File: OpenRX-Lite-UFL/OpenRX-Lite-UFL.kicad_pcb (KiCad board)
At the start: 6 copper layers, 8.5 x 12.3 mm, 39 parts, among them U1 ESP32-C3FH4, U2 TLV75533PDQNR, U3 SX1281IMLTRT, X1 CJ17-400001010B20

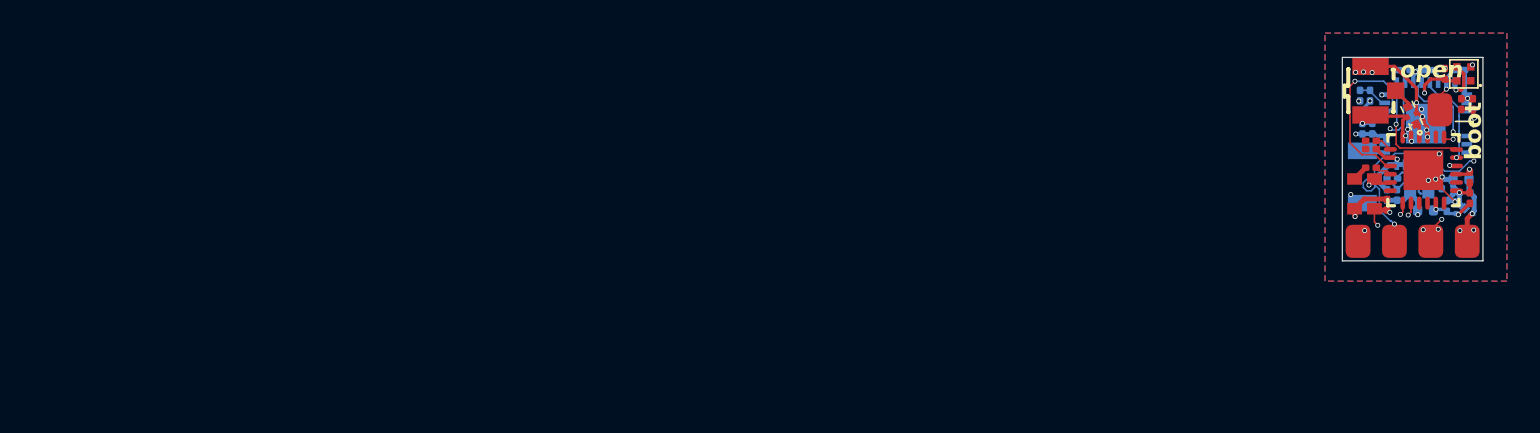
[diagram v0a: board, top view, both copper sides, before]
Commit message: OpenRX Lite (UFL + molex)
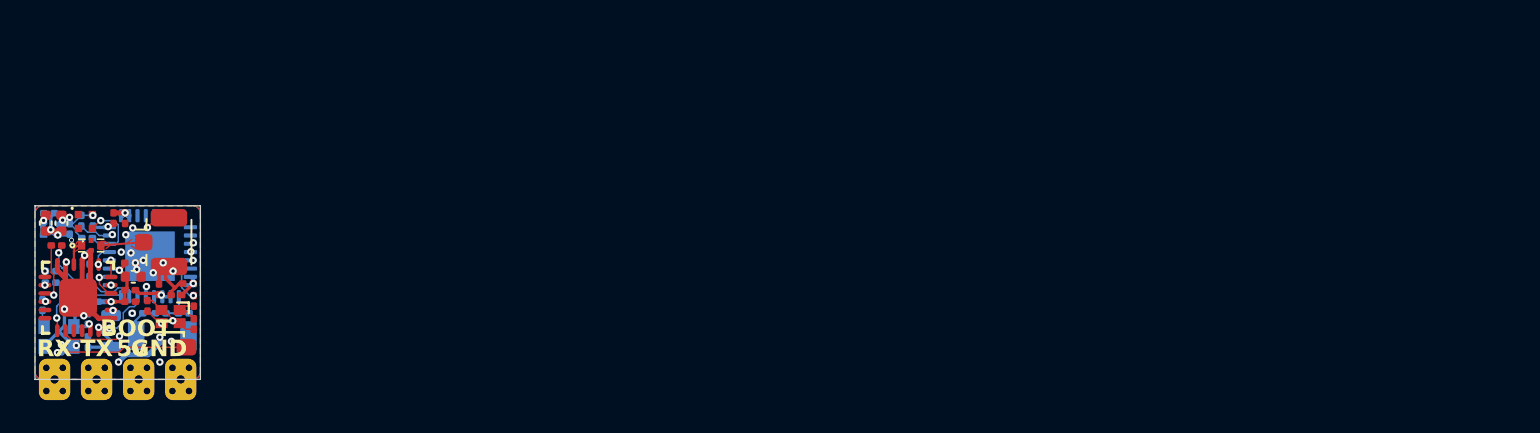
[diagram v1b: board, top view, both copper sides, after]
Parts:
- removed C18, C7: 100nF, Capacitor_SMD:C_0201_0603Metric
- removed C2: 1uF, Capacitor_SMD:C_0201_0603Metric
- removed JP1: U.FL-R-SMT-1(80), OpenRX-Shared:RF-SMD_FRF05002-JSS103M
- removed R1: 10k, Resistor_SMD:R_0201_0603Metric
- added C21: 1.2pF, Capacitor_SMD:C_0201_0603Metric, B.Cu at (106.2, 106.0)
- added C22: 1.2pF, Capacitor_SMD:C_0201_0603Metric, B.Cu at (109.0, 106.0)
- added C23: 1uF, Capacitor_SMD:C_0201_0603Metric, F.Cu at (105.5, 100.2)
- added C24: 10nF, Capacitor_SMD:C_0201_0603Metric, F.Cu at (109.2, 104.2)
- added C25: 1uF, Capacitor_SMD:C_0201_0603Metric, F.Cu at (107.5, 104.5)
- added C26: 10nF, Capacitor_SMD:C_0201_0603Metric, B.Cu at (101.0, 104.2)
- added C27: 10nF, Capacitor_SMD:C_0201_0603Metric, B.Cu at (101.0, 103.5)
- added C28: 1uF, Capacitor_SMD:C_0201_0603Metric, B.Cu at (103.3, 102.7)
- added J1: Conn_Coaxial, Connector_Coaxial:U.FL_Hirose_U.FL-R-SMT-1_Vertical, F.Cu at (108.1, 101.7)
- added L2: 2.5nH, Inductor_SMD:L_0201_0603Metric, B.Cu at (107.6, 106.0)
- added L3: 2.0nH, Inductor_SMD:L_0201_0603Metric, F.Cu at (105.8, 104.6)
- added L4: 15uH, Inductor_SMD:L_0805_2012Metric, B.Cu at (104.6, 107.1)
- added R5: 10k, Resistor_SMD:R_0201_0603Metric, B.Cu at (103.3, 104.1)
- C1, C3: value 18pF -> 15pF; moved to F.Cu
- C11: value 100nF -> 10uF; footprint Capacitor_SMD:C_0201_0603Metric -> Capacitor_SMD:C_0402_1005Metric
- C13, C14, C17, C19, C20, OSC1: moved to B.Cu
- C16, C4, C5, C6, C8, L1, R2, X1: moved to F.Cu
- TP5: value GND -> BOOT
- U1: value ESP32-C3FH4 -> ESP32-C3; footprint OpenRX-Shared:QFN-32_L5.0-W5.0-P0.50-TL-EP3.7 -> Package_DFN_QFN:QFN-32-1EP_5x5mm_P0.5mm_EP3.7x3.7mm
- moved C8 85.6 mm to (100.7, 100.5), turned to -90 degrees
- moved C10 85.6 mm to (100.8, 100.0), turned to 0 degrees
- moved U2 85.5 mm to (101.0, 101.0), turned to 180 degrees
- moved D1 83.8 mm to (103.0, 100.5), turned to 0 degrees
- moved R4 83.8 mm to (102.8, 100.4), turned to -90 degrees
- moved C17 83.6 mm to (103.5, 105.3), turned to 180 degrees
- moved C15 83.3 mm to (102.1, 100.9), turned to -90 degrees
- moved C16 82.5 mm to (101.6, 100.5), turned to -90 degrees
- moved C9 82.1 mm to (105.8, 105.3), turned to 0 degrees
- moved R3 81.7 mm to (103.2, 101.5)
- moved U3 81.7 mm to (102.6, 105.0)
- moved C11 81.0 mm to (105.9, 103.8), turned to 0 degrees
- moved TP3 80.8 mm to (106.3, 110.0), turned to 0 degrees
- moved C19 80.8 mm to (100.5, 105.5), turned to 90 degrees
- moved FL1 80.2 mm to (103.4, 101.9), turned to 0 degrees
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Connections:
- net /ESP32-C3 + SX1281 Core (UFL)/CHIP_BOOT renamed /ESP32-C3 + SX1281 Core (UFL)/BOOT
- C20 pad 1: Net-(U3-VR_PA) -> GND
- C20 pad 2: GND -> Net-(U3-DCC_FB)
- D1 pad 2: +5V -> +3V3
- R3 pad 2: /ESP32-C3 + SX1281 Core (UFL)/NSS -> /ESP32-C3 + SX1281 Core (UFL)/LED
- U1 pad 1: /ESP32-C3 + SX1281 Core (UFL)/WIFI -> Net-(U1-LNA_IN)
- U1 pad 10: /ESP32-C3 + SX1281 Core (UFL)/DIO1 -> /ESP32-C3 + SX1281 Core (UFL)/MISO
- U1 pad 12: /ESP32-C3 + SX1281 Core (UFL)/MISO -> /ESP32-C3 + SX1281 Core (UFL)/SCK
- U1 pad 13: /ESP32-C3 + SX1281 Core (UFL)/MOSI -> /ESP32-C3 + SX1281 Core (UFL)/NSS
- U1 pad 14: /ESP32-C3 + SX1281 Core (UFL)/NSS -> /ESP32-C3 + SX1281 Core (UFL)/LED
- U1 pad 16: /ESP32-C3 + SX1281 Core (UFL)/LED -> GND
- U1 pad 2: +3V3 -> Net-(C25-Pad1)
- U1 pad 3: +3V3 -> Net-(C25-Pad1)
- U1 pad 9: /ESP32-C3 + SX1281 Core (UFL)/SCK -> /ESP32-C3 + SX1281 Core (UFL)/MOSI
- U3 pad 12: unconnected-(U3-DCC_FB-Pad12) -> Net-(U3-DCC_FB)
- U3 pad 14: unconnected-(U3-DCC_SW-Pad14) -> Net-(U3-DCC_SW)
- U3 pad 2: +3V3 -> Net-(U3-DCC_FB)
- U3 pad 5: GND -> unconnected-(U3-GND-Pad5)
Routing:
- net /ESP32-C3 + SX1281 Core (UFL)/BOOT: track 2.76 -> 19.5 mm, vias 1 -> 2
- net GND: track 46.3 -> 32.1 mm, vias 29 -> 25
- net Net-(U3-DCC_FB): track 0.00 -> 7.68 mm, vias 0 -> 2
- net /ESP32-C3 + SX1281 Core (UFL)/SCK: track 7.53 -> 1.02 mm
- net /ESP32-C3 + SX1281 Core (UFL)/NSS: track 7.45 -> 1.53 mm, vias 2 -> 1
- net /ESP32-C3 + SX1281 Core (UFL)/MOSI: track 5.63 -> 0.10 mm
- net /ESP32-C3 + SX1281 Core (UFL)/MISO: track 7.04 -> 1.98 mm, vias 2 -> 1
- net +5V: track 17.1 -> 13.7 mm, vias 4 -> 1
- net /ESP32-C3 + SX1281 Core (UFL)/BUSY: track 8.60 -> 5.50 mm, vias 2 -> 1
- net /ESP32-C3 + SX1281 Core (UFL)/XTAL_N: track 3.28 -> 5.89 mm, vias 0 -> 2
- net /ESP32-C3 + SX1281 Core (UFL)/CHIP_EN: track 1.80 -> 4.21 mm
- net Net-(C25-Pad1): track 0.00 -> 2.30 mm, vias 0 -> 1
- net /ESP32-C3 + SX1281 Core (UFL)/LED: track 2.43 -> 4.65 mm
- net /ESP32-C3 + SX1281 Core (UFL)/DIO1: track 10.0 -> 8.22 mm
- net Net-(U1-LNA_IN): track 0.00 -> 1.77 mm
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- added copper zone on In2.Cu, net +3V3
- added copper zone on In3.Cu, net GND
- added copper zone on F.Cu, net Net-(FL1-IN)
- added copper zone on F.Cu, net Net-(FL1-OUT)
- removed copper zone on In3.Cu, net +3V3
- removed copper zone on In2.Cu, net GND
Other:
- board size 8.5 x 12.3 mm -> 10 x 10.5 mm
- board text added: "BOOT"
- board text removed: "boot"
